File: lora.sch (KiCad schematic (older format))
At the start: 53 parts, among them J1 Conn_01x02, J10 Conn, J11 Conn_Coaxial, J2 Humidity, J3 Temp, J4 Programming_Jumper, J5 Temp, J6 VDD, J7 GPS, J8 SIM800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

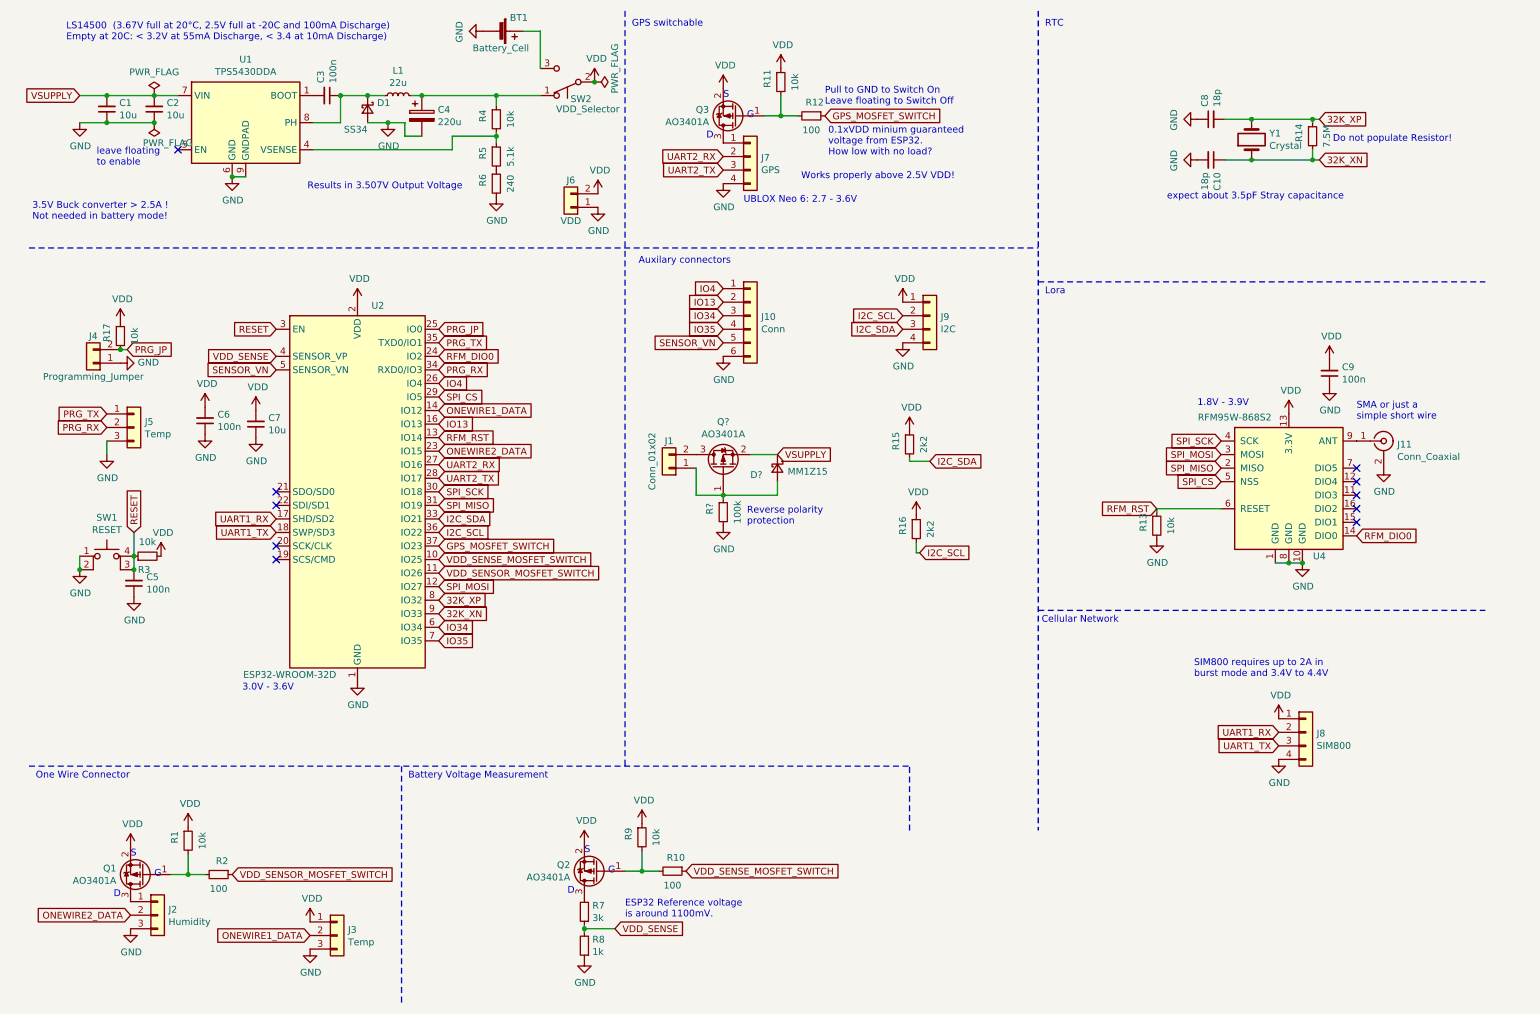
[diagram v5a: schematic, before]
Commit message: added reverse polarity protection for battery.
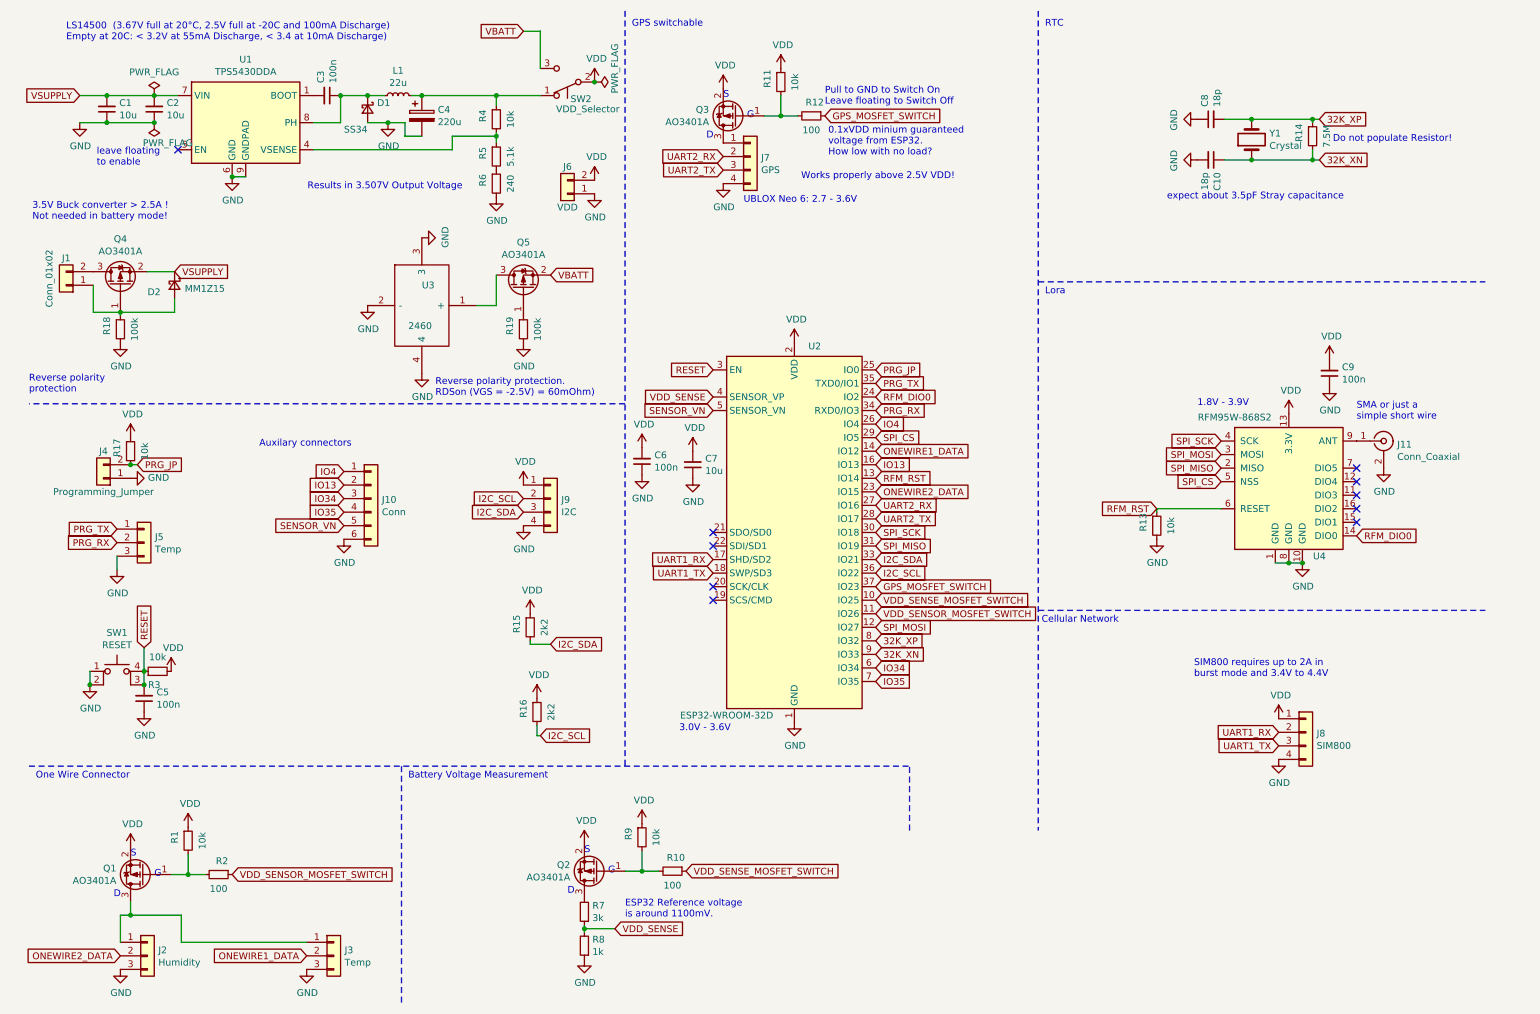
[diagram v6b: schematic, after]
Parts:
- removed BT1: Battery_Cell, symbol Device:Battery_Cell
- added Q5: AO3401A, Package_TO_SOT_SMD:SOT-23, symbol Transistor_FET:AO3401A
- added R19: 100k, Resistor_SMD:R_0603_1608Metric, symbol Device:R_Small
- added U3: 2460, 2460, symbol SamacSys_Parts:2460
- C1, C2, C7: footprint (none) -> Capacitor_SMD:C_0805_2012Metric; LCSC (none) -> C15850
- C3, C5, C6, C9: footprint (none) -> Capacitor_SMD:C_0603_1608Metric; LCSC (none) -> C14663
- D1: footprint (none) -> Diode_SMD:D_SMA
- D2: renamed from D?; footprint (none) -> Diode_SMD:D_SOD-123; LCSC C86235 -> C86235
- J1, J4, J6: footprint (none) -> Connector_PinHeader_2.54mm:PinHeader_1x02_P2.54mm_Vertical
- J10: footprint (none) -> Connector_PinHeader_2.54mm:PinHeader_1x06_P2.54mm_Vertical
- J11: footprint (none) -> Connector_Coaxial:SMA_Amphenol_132134_Vertical
- J2, J3, J5, SW2: footprint (none) -> Connector_PinHeader_2.54mm:PinHeader_1x03_P2.54mm_Vertical
- J7, J8, J9: footprint (none) -> Connector_PinHeader_2.54mm:PinHeader_1x04_P2.54mm_Vertical
- L1: footprint (none) -> OWN_Parts_:L_MS1040-220M
- Q1, Q2, Q3: LCSC (none) -> C15127
- Q4: renamed from Q?; LCSC (none) -> C15127
- R1, R11, R13, R17, R3, R4, R9: footprint (none) -> Capacitor_SMD:C_0603_1608Metric; LCSC (none) -> C25804
- R10, R12, R2: footprint (none) -> Resistor_SMD:R_0603_1608Metric; LCSC (none) -> C22775
- R15, R16: footprint (none) -> Resistor_SMD:R_0603_1608Metric; LCSC (none) -> C4190
- R18: renamed from R?; footprint (none) -> Resistor_SMD:R_0603_1608Metric; LCSC (none) -> C25803
- R7: footprint (none) -> Resistor_SMD:R_0603_1608Metric; LCSC C4211 -> C4211
- R8: footprint (none) -> Resistor_SMD:R_0603_1608Metric
- SW1: footprint (none) -> OWN_Parts_:TS-1187A-C-E-B; LCSC (none) -> C318889
- U4: footprint (none) -> RF_Module:HOPERF_RFM9XW_SMD
- Y1: footprint (none) -> Crystal:Crystal_SMD_MicroCrystal_CC7V-T1A-2Pin_3.2x1.5mm
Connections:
- net GND: now also R19.2, U3.2 (-), U3.3, U3.4
- net VDD: no longer J3.1 (Pin_1)
- net VBATT: now reaches SW2.3 (C)
- net VBATT: now also Q5.2 (S)
- net at J2.1 (Pin_1), Q1.3 (D): now also J3.1 (Pin_1)
- new net: Q5.3 (D), U3.1 (+)
- new net: Q5.1 (G), R19.1
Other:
- note added: "Reverse polarity protection. \nRDSon (VGS = -2.5V) = 60mOhm)"
- moved on the sheet: C5, C6, C7, D2, J1, J10, J2, J3, J4, J5, J6, J9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
